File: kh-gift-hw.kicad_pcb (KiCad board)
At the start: 2 copper layers, 89.3 x 55 mm, 69 parts, among them J2 Conn_01x14, J3 USB, Q1 MMBT5550, Q4 MMBT2222A, Q5 MMBT2222A, SW1 SW_Push, SW2 SW_Push, SW3 SW_Push, U1 DHT11, U10 IRLML0030, U12 IRLML0030, U2 ESP32-WROVER, U3 TP4056, U4 DW01A, U6 CP2102N-Axx-xQFN28, U7 SX1308, U8 AMS1117-3.3, U9 DS1307Z+, Y1 32768 kHz

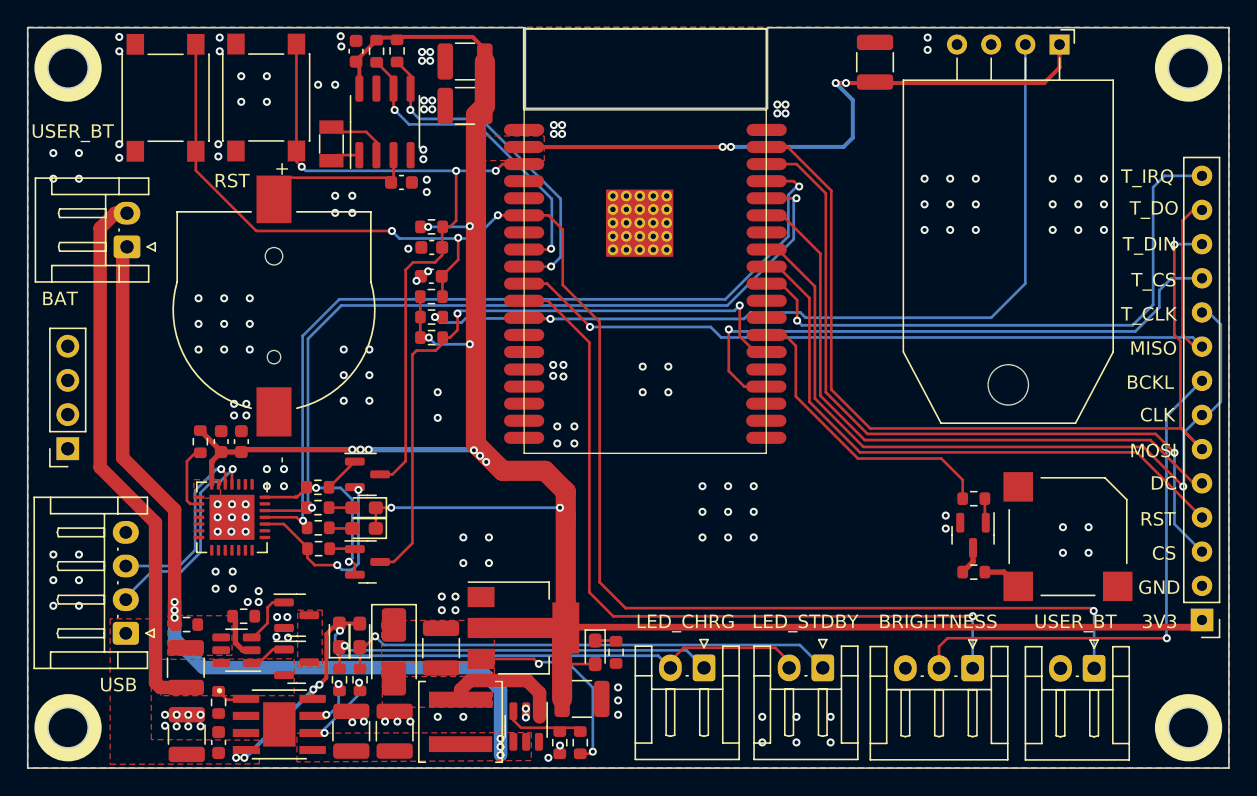
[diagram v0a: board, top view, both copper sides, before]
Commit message: add USB pinout description
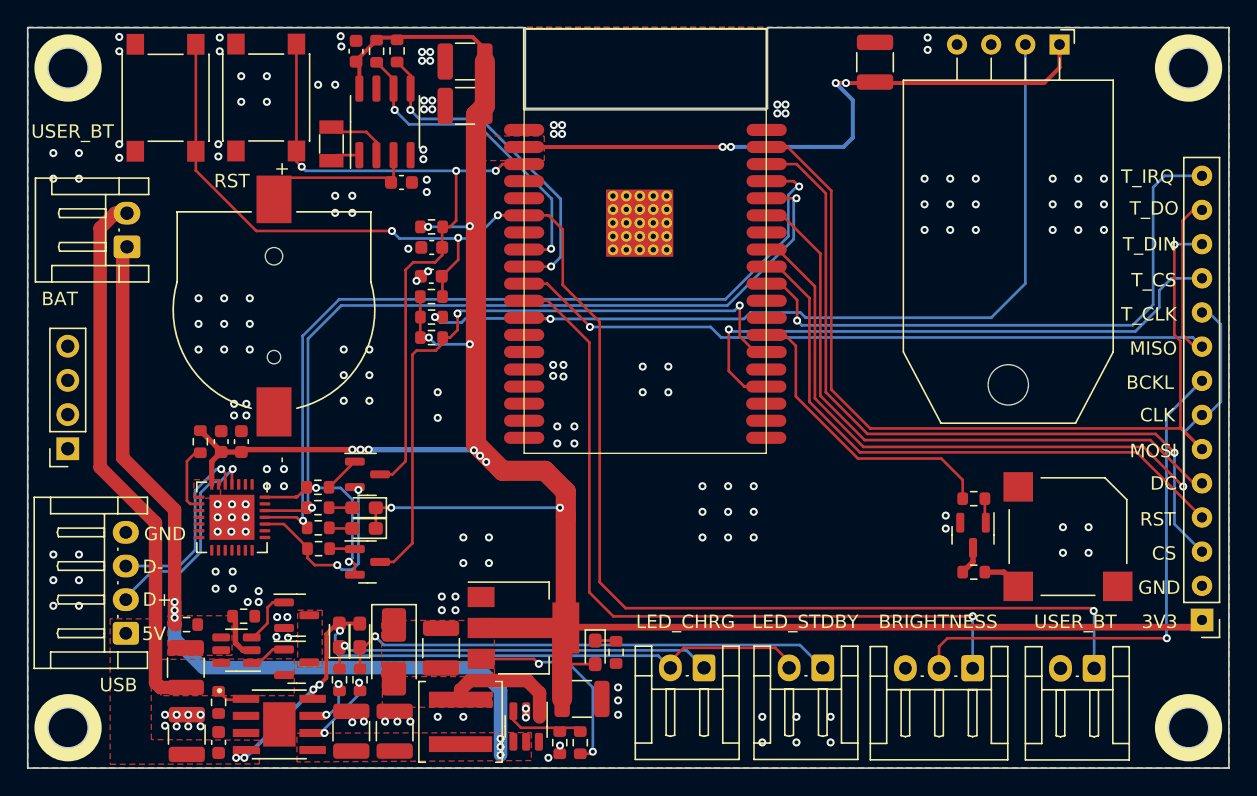
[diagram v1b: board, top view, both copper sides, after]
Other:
- board text added: "5V"
- board text added: "D+"
- board text added: "D-"
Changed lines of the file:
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@@
     (fp_line (start -0.32 -1.59) (end -0.32 -5.01)
       (stroke (width 0.12) (type solid)) (layer "F.SilkS"))
-    (fp_line (start -0.3 2.1) (end 0.3 2.1)
-      (stroke (width 0.12) (type solid)) (layer "F.SilkS"))
     (fp_line (start 0 -5.09) (end 0.32 -5.01)
       (stroke (width 0.12) (type solid)) (layer "F.SilkS"))
     (fp_line (start 0 -1.59) (end -0.32 -1.59)
       (stroke (width 0.12) (type solid)) (layer "F.SilkS"))
-    (fp_line (start 0 1.5) (end -0.3 2.1)
-      (stroke (width 0.12) (type solid)) (layer "F.SilkS"))
-    (fp_line (start 0.3 2.1) (end 0 1.5)
-      (stroke (width 0.12) (type solid)) (layer "F.SilkS"))
     (fp_line (start 0.32 -5.01) (end 0.32 -1.59)
       (stroke (width 0.12) (type solid)) (layer "F.SilkS"))
@@
         (effects (font (size 1 1) (thickness 0.05)))
     )
-    (fp_text user "-" (at -11.14 0.52 90) (layer "F.SilkS")
+    (fp_text user "+" (at 10.49 0.57 90) (layer "F.SilkS")
         (effects (font (size 1 1) (thickness 0.05)))
     )
-    (fp_text user "+" (at 10.49 0.57 90) (layer "F.SilkS")
+    (fp_text user "-" (at -11.14 0.52 90) (layer "F.SilkS")
         (effects (font (size 1 1) (thickness 0.05)))
     )
@@
         (effects (font (size 1 1) (thickness 0.15)))
     )
-    (fp_text user "${REFERENCE}" (at 0 2.5 90 unlocked) (layer "F.Fab")
+    (fp_text user "${REFERENCE}" (at 1.25 -2.6 90) (layer "F.Fab")
         (effects (font (size 1 1) (thickness 0.15)))
     )
-    (fp_text user "${REFERENCE}" (at 1.25 -2.6 90) (layer "F.Fab")
+    (fp_text user "${REFERENCE}" (at 0 2.5 90 unlocked) (layer "F.Fab")
         (effects (font (size 1 1) (thickness 0.15)))
     )
@@
     (fp_line (start -0.32 -1.59) (end -0.32 -5.01)
       (stroke (width 0.12) (type solid)) (layer "F.SilkS"))
-    (fp_line (start -0.3 2.1) (end 0.3 2.1)
-      (stroke (width 0.12) (type solid)) (layer "F.SilkS"))
     (fp_line (start 0 -5.09) (end 0.32 -5.01)
       (stroke (width 0.12) (type solid)) (layer "F.SilkS"))
     (fp_line (start 0 -1.59) (end -0.32 -1.59)
       (stroke (width 0.12) (type solid)) (layer "F.SilkS"))
-    (fp_line (start 0 1.5) (end -0.3 2.1)
-      (stroke (width 0.12) (type solid)) (layer "F.SilkS"))
-    (fp_line (start 0.3 2.1) (end 0 1.5)
-      (stroke (width 0.12) (type solid)) (layer "F.SilkS"))
     (fp_line (start 0.32 -5.01) (end 0.32 -1.59)
       (stroke (width 0.12) (type solid)) (layer "F.SilkS"))
@@
     (fp_line (start -0.32 -1.59) (end -0.32 -5.01)
       (stroke (width 0.12) (type solid)) (layer "F.SilkS"))
-    (fp_line (start -0.3 2.1) (end 0.3 2.1)
-      (stroke (width 0.12) (type solid)) (layer "F.SilkS"))
     (fp_line (start 0 -5.09) (end 0.32 -5.01)
       (stroke (width 0.12) (type solid)) (layer "F.SilkS"))
     (fp_line (start 0 -1.59) (end -0.32 -1.59)
       (stroke (width 0.12) (type solid)) (layer "F.SilkS"))
-    (fp_line (start 0 1.5) (end -0.3 2.1)
-      (stroke (width 0.12) (type solid)) (layer "F.SilkS"))
-    (fp_line (start 0.3 2.1) (end 0 1.5)
-      (stroke (width 0.12) (type solid)) (layer "F.SilkS"))
     (fp_line (start 0.32 -5.01) (end 0.32 -1.59)
       (stroke (width 0.12) (type solid)) (layer "F.SilkS"))
@@
     (fp_line (start -0.32 -1.59) (end -0.32 -5.01)
       (stroke (width 0.12) (type solid)) (layer "F.SilkS"))
-    (fp_line (start -0.3 2.1) (end 0.3 2.1)
-      (stroke (width 0.12) (type solid)) (layer "F.SilkS"))
     (fp_line (start 0 -5.09) (end 0.32 -5.01)
       (stroke (width 0.12) (type solid)) (layer "F.SilkS"))
     (fp_line (start 0 -1.59) (end -0.32 -1.59)
       (stroke (width 0.12) (type solid)) (layer "F.SilkS"))
-    (fp_line (start 0 1.5) (end -0.3 2.1)
-      (stroke (width 0.12) (type solid)) (layer "F.SilkS"))
-    (fp_line (start 0.3 2.1) (end 0 1.5)
-      (stroke (width 0.12) (type solid)) (layer "F.SilkS"))
     (fp_line (start 0.32 -5.01) (end 0.32 -1.59)
       (stroke (width 0.12) (type solid)) (layer "F.SilkS"))
@@
         (effects (font (size 1 1) (thickness 0.15)))
     )
-    (fp_text user "${REFERENCE}" (at 0 -4.05 90) (layer "F.Fab")
+    (fp_text user "${REFERENCE}" (at 0 2.5 -90 unlocked) (layer "F.Fab")
         (effects (font (size 1 1) (thickness 0.15)))
     )
-    (fp_text user "${REFERENCE}" (at 0 2.5 -90 unlocked) (layer "F.Fab")
+    (fp_text user "${REFERENCE}" (at 0 -4.05 90) (layer "F.Fab")
         (effects (font (size 1 1) (thickness 0.15)))
     )
@@
         (effects (font (size 1 1) (thickness 0.15)))
     )
-    (fp_text user "${REFERENCE}" (at 0 2.5 90 unlocked) (layer "F.Fab")
+    (fp_text user "${REFERENCE}" (at 3.75 -2.6 90) (layer "F.Fab")
         (effects (font (size 1 1) (thickness 0.15)))
     )
-    (fp_text user "${REFERENCE}" (at 3.75 -2.6 90) (layer "F.Fab")
+    (fp_text user "${REFERENCE}" (at 0 2.5 90 unlocked) (layer "F.Fab")
         (effects (font (size 1 1) (thickness 0.15)))
     )
@@
     (fp_line (start -0.32 -1.59) (end -0.32 -5.01)
       (stroke (width 0.12) (type solid)) (layer "F.SilkS"))
-    (fp_line (start -0.3 2.1) (end 0.3 2.1)
-      (stroke (width 0.12) (type solid)) (layer "F.SilkS"))
     (fp_line (start 0 -5.09) (end 0.32 -5.01)
       (stroke (width 0.12) (type solid)) (layer "F.SilkS"))
     (fp_line (start 0 -1.59) (end -0.32 -1.59)
       (stroke (width 0.12) (type solid)) (layer "F.SilkS"))
-    (fp_line (start 0 1.5) (end -0.3 2.1)
-      (stroke (width 0.12) (type solid)) (layer "F.SilkS"))
-    (fp_line (start 0.3 2.1) (end 0 1.5)
-      (stroke (width 0.12) (type solid)) (layer "F.SilkS"))
     (fp_line (start 0.32 -5.01) (end 0.32 -1.59)
       (stroke (width 0.12) (type solid)) (layer "F.SilkS"))
@@
         (effects (font (size 1 1) (thickness 0.15)))
     )
-    (fp_text user "${REFERENCE}" (at 1.25 -2.6) (layer "F.Fab")
+    (fp_text user "${REFERENCE}" (at 0 2.5 180 unlocked) (layer "F.Fab")
         (effects (font (size 1 1) (thickness 0.15)))
     )
-    (fp_text user "${REFERENCE}" (at 0 2.5 180 unlocked) (layer "F.Fab")
+    (fp_text user "${REFERENCE}" (at 1.25 -2.6) (layer "F.Fab")
         (effects (font (size 1 1) (thickness 0.15)))
     )
@@
     (fp_line (start -0.32 -1.59) (end -0.32 -5.01)
       (stroke (width 0.12) (type solid)) (layer "F.SilkS"))
-    (fp_line (start -0.3 2.1) (end 0.3 2.1)
-      (stroke (width 0.12) (type solid)) (layer "F.SilkS"))
     (fp_line (start 0 -5.09) (end 0.32 -5.01)
       (stroke (width 0.12) (type solid)) (layer "F.SilkS"))
     (fp_line (start 0 -1.59) (end -0.32 -1.59)
       (stroke (width 0.12) (type solid)) (layer "F.SilkS"))
-    (fp_line (start 0 1.5) (end -0.3 2.1)
-      (stroke (width 0.12) (type solid)) (layer "F.SilkS"))
-    (fp_line (start 0.3 2.1) (end 0 1.5)
-      (stroke (width 0.12) (type solid)) (layer "F.SilkS"))
     (fp_line (start 0.32 -5.01) (end 0.32 -1.59)
       (stroke (width 0.12) (type solid)) (layer "F.SilkS"))
@@
     (effects (font (size 1 1) (thickness 0.15)) (justify left bottom))
   )
+  (gr_text "GND" (at 41.123 130.7227) (layer "F.SilkS")
+    (effects (font (size 1 1) (thickness 0.15)) (justify left bottom))
+  )
+  (gr_text "D-" (at 41.0214 133.1611) (layer "F.SilkS")
+    (effects (font (size 1 1) (thickness 0.15)) (justify left bottom))
+  )
   (gr_text "3V3" (at 115.291 137.2505) (layer "F.SilkS")
     (effects (font (size 1 1) (thickness 0.15)) (justify left bottom))
@@
     (effects (font (size 1 1) (thickness 0.15)) (justify left bottom))
   )
+  (gr_text "D+" (at 41.0214 135.5995) (layer "F.SilkS")
+    (effects (font (size 1 1) (thickness 0.15)) (justify left bottom))
+  )
   (gr_text "T_IRQ" (at 113.767 104.1543) (layer "F.SilkS")
     (effects (font (size 1 1) (thickness 0.15)) (justify left bottom))
@@
     (effects (font (size 1 1) (thickness 0.15)) (justify left bottom))
   )
+  (gr_text "5V" (at 40.9706 138.1395) (layer "F.SilkS")
+    (effects (font (size 1 1) (thickness 0.15)) (justify left bottom))
+  )

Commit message: update project setting for Kicad v8
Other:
- rule pad_to_mask_clearance: 0.05 -> 0

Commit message: update project
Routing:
- net +3V3: track 224.3 -> 217.3 mm
- net Net-(BT1-+): track 63.2 -> 63.1 mm, vias 6 -> 5
- net GND: vias 181 -> 174

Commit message: update footprint
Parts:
- BT2: footprint footprints:BAT_CR1220_Holder -> Footprint-Kicad:BAT_CR1220_Holder
- D5, D6, SW3: footprint footprints:JST_EH_S2B-EH_1x02_P2.5mm_Horizontal -> Footprint-Kicad:Connector_ZH_1x02_P1.25mm_Horizontal
- RV1: footprint footprints:JST_EH_S3B-EH_1x03_P2.5mm_Horizontal -> Footprint-Kicad:Connector_ZH_1x03_P1.25mm_Horizontal
- U2: footprint footprints:ESP32-WROVER -> Footprint-Kicad:ESP32-WROVER
